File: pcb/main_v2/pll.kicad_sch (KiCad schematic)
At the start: 52 parts, among them U601 ADF4351, U602 XMB0220K1-50100G, U603 PD0922J5050D2HF, Y601 ATX-11-F-26.000MHZ-F05-T

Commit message: updarted schematic and simulation
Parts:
- removed R617: 100, Resistor_SMD:R_0402_1005Metric, symbol Device:R
- removed R618: 200, Resistor_SMD:R_0402_1005Metric, symbol Device:R
- removed U602: XMB0220K1-50100G, My Footprints:XMB0220K1-50100G_TTT, symbol My Symbols:XMB0220K1-50100G
- removed U603: PD0922J5050D2HF, PD0922J5050D2HF, symbol My Symbols:PD0922J5050D2HF
- added C501: 0.1 uF, Capacitor_SMD:C_0402_1005Metric, symbol Device:C
- added C502: 10 pF, Capacitor_SMD:C_0402_1005Metric, symbol Device:C
- added C503: 120 pF, Capacitor_SMD:C_0402_1005Metric, symbol Device:C
- Y601: footprint ATX11F26000MHZF05T -> My Footprints:ATX11F26000MHZF05T
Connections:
- net Vout is gone; now on net +3.3V: C611.1, C612.2, C626.1, L601.1, L602.1
- net +3.3V: now also C501.1, C502.1, C503.2
- net GND: now also C501.2, C502.2, C503.1
- net OX Out + renamed Oscillator +
- net OX Out - renamed Oscillator -
- net RF In renamed TCXO
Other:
- note removed: "Balun 1:2"
- note removed: "Power Splitter"
- note removed: "TODO: calculate loop filter. Welche Bandbreite?"
- moved on the sheet: C613, C627, C628, R605, Y601

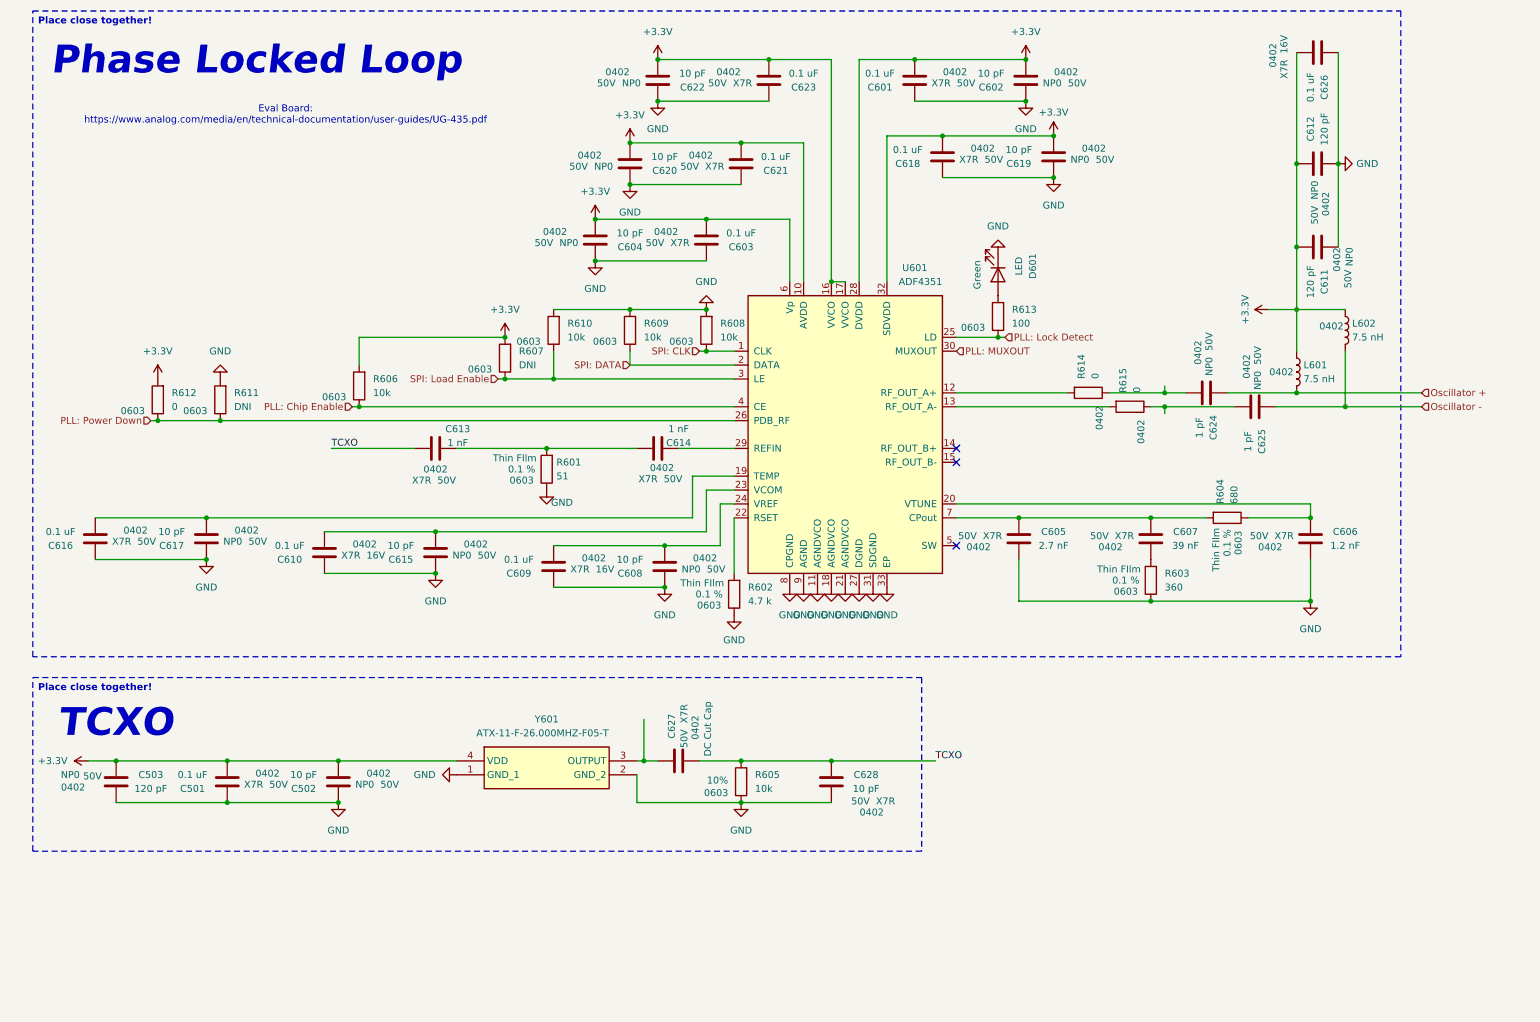
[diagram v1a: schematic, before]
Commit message: updated io schematic
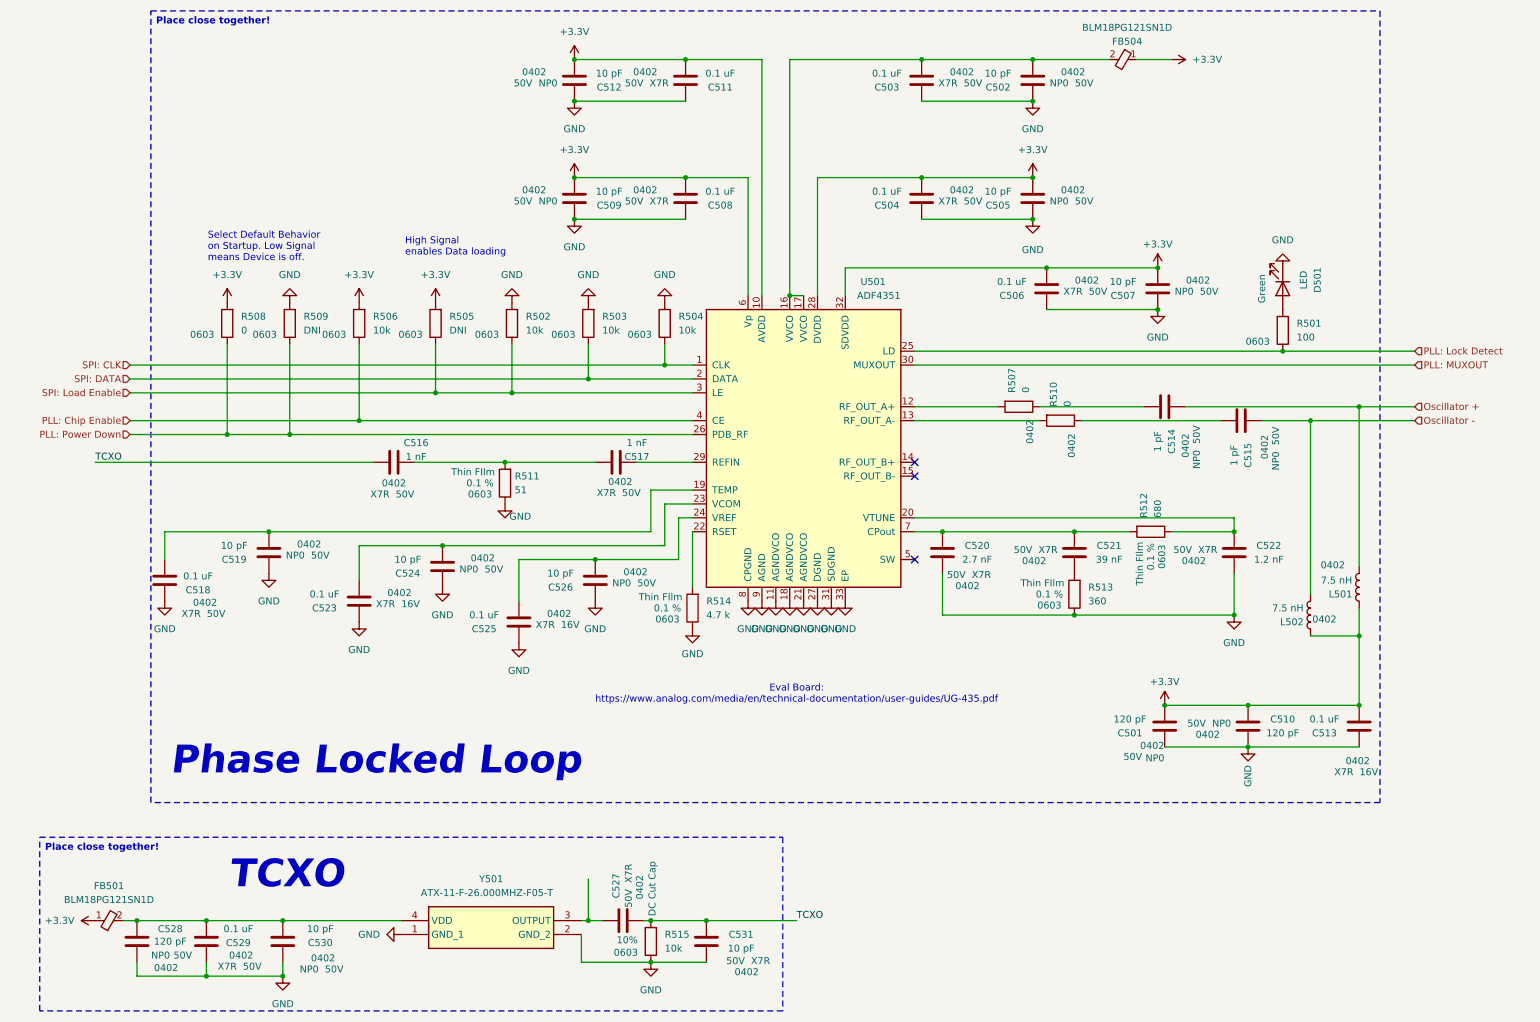
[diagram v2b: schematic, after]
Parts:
- removed C603, C621, C623, C626: 0.1 uF, Capacitor_SMD:C_0402_1005Metric, symbol Device:C
- removed C604, C620, C622: 10 pF, Capacitor_SMD:C_0402_1005Metric, symbol Device:C
- removed C611, C612: 120 pF, Capacitor_SMD:C_0402_1005Metric, symbol Device:C
- removed L601, L602: 7.5 nH, Inductor_SMD:L_0402_1005Metric, symbol Device:L
- added C501, C510: 120 pF, Capacitor_SMD:C_0402_1005Metric, symbol Device:C
- added C502, C509, C512: 10 pF, Capacitor_SMD:C_0402_1005Metric, symbol Device:C
- added C503, C508, C511, C513: 0.1 uF, Capacitor_SMD:C_0402_1005Metric, symbol Device:C
- added FB501, FB504: BLM18PG121SN1D, BLM18SP221SN1B, symbol My Symbols:BLM18PG121SN1D
- added L501, L502: 7.5 nH, Inductor_SMD:L_0402_1005Metric, symbol Device:L
- renumbered C601 to C504, C602 to C505, C618 to C506, C619 to C507, C624 to C514, C625 to C515, C613 to C516, C614 to C517, C616 to C518, C617 to C519, C605 to C520, C607 to C521, C606 to C522, C610 to C523, C615 to C524, C609 to C525, C608 to C526, C627 to C527, C503 to C528, C501 to C529, C502 to C530, C628 to C531, D601 to D501, R613 to R501, R610 to R502, R609 to R503, R608 to R504, R607 to R505, R606 to R506, R614 to R507, R612 to R508, R611 to R509, R615 to R510, R601 to R511, R604 to R512, R603 to R513, R602 to R514, R605 to R515, U601 to U501, Y601 to Y501
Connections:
- net +3.3V: now also C501.1, C508.1, C509.1, C510.2, C511.1, C512.1, C513.1, FB501.1, FB504.1, L501.1, L502.1; no longer C528.2, C529.1, C530.1, U501.16 (VVCO), U501.17 (VVCO), Y501.4 (VDD)
- net GND: now also C501.2, C502.2, C503.2, C508.2, C509.2, C510.1, C511.2, C512.2, C513.2
- net Oscillator +: now also L501.2
- net Oscillator -: now also L502.2
- new net: C502.1, C503.1, FB504.2, U501.16 (VVCO), U501.17 (VVCO)
- new net: C528.2, C529.1, C530.1, FB501.2, Y501.4 (VDD)
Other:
- note added: "High Signal enables Data loading"
- note added: "Select Default Behavior on Startup. Low Signal means Device is off."
- moved on the sheet: C504, C505, C506, C507, C514, C515, C516, C517, C518, C519, C520, C521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

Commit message: update bom
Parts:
- FB501: renamed from FB504; footprint BLM18SP221SN1B -> My Footprints:BLM18SP221SN1B
- FB502: renamed from FB501; footprint BLM18SP221SN1B -> My Footprints:BLM18SP221SN1B
- renumbered C512 to C501, C511 to C502, C502 to C504, C509 to C505, C508 to C506, C504 to C507, C505 to C508, C506 to C509, C507 to C510, C514 to C511, C515 to C512, C516 to C513, C517 to C514, C519 to C515, C520 to C516, C521 to C517, C522 to C518, C524 to C519, C518 to C520, C526 to C521, C523 to C522, C525 to C523, C501 to C524, C510 to C525, C513 to C526, R508 to R501, R509 to R502, R506 to R503, R505 to R504, R502 to R505, R503 to R506, R504 to R507, R501 to R508, R507 to R509

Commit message: updated layout
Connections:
- net Ox Blocked -: now reaches C512.1, R510.1
- net Ox +: now reaches R509.2, U501.12 (RF_OUT_A+)
- net Ox -: now reaches R510.2, U501.13 (RF_OUT_A-)
- net Ox Blocked +: now reaches C511.1, R509.1
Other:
- moved on the sheet: C511, C512

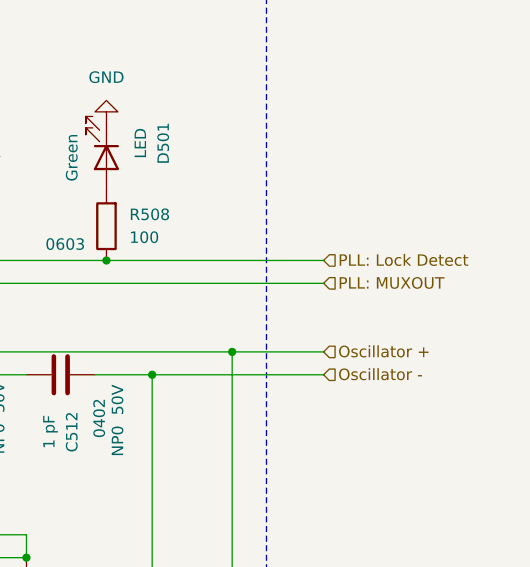
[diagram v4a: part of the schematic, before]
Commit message: updated spi connection
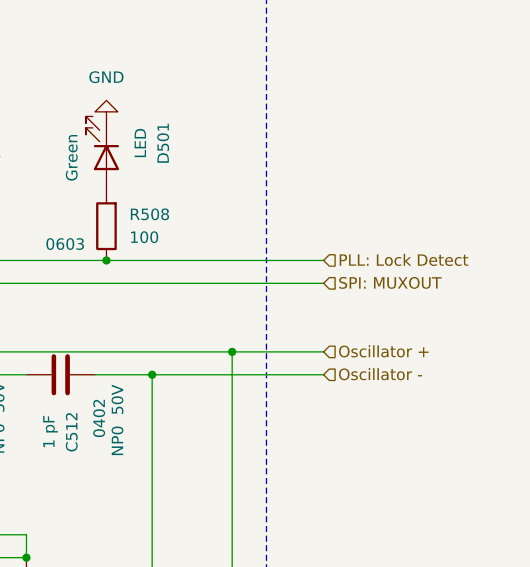
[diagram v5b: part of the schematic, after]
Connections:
- net PLL: MUXOUT renamed SPI: MUXOUT
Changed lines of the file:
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@@
 		)
 	)
-	(hierarchical_label "PLL: MUXOUT"
+	(hierarchical_label "SPI: MUXOUT"
 		(shape input)
 		(at 266.7 77.47 0)

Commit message: added second LNA
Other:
- note added: "Place Thermal Vias for Heat Dissapation!"
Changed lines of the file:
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@@
 		)
 	)
+	(text "Place Thermal Vias for Heat Dissapation!"
+		(exclude_from_sim no)
+		(at 62.738 26.162 0)
+		(effects
+			(font
+				(size 1.27 1.27)
+			)
+		)
+	)
 	(text "High Signal \nenables Data loading\n"
 		(exclude_from_sim no)
@@
 					(unit 1)
 				)
+			)
+		)
+	)
+	(symbol
+		(lib_id "Graphic:SYM_Hot_Small")
+		(at 62.23 30.48 0)
+		(unit 1)
+		(body_style 1)
+		(exclude_from_sim yes)
+		(in_bom no)
+		(on_board no)
+		(in_pos_files yes)
+		(dnp no)
+		(fields_autoplaced yes)
+		(property "Reference" "#SYM501"
+			(at 62.23 26.924 0)
+			(hide yes)
+			(show_name no)
+			(do_not_autoplace no)
+			(effects
+				(font
+					(size 1.27 1.27)
+				)
+			)
+		)
+		(property "Value" "SYM_Hot_Small"
+			(at 62.23 33.655 0)
+			(hide yes)
+			(show_name no)
+			(do_not_autoplace no)
+			(effects
+				(font
+					(size 1.27 1.27)
+				)
+			)
+		)
+		(property "Footprint" ""
+			(at 62.23 34.925 0)
+			(hide yes)
+			(show_name no)
+			(do_not_autoplace no)
+			(effects
+				(font
+					(size 1.27 1.27)
+				)
+			)
+		)
+		(property "Datasheet" ""
+			(at 62.992 35.56 0)
+			(hide yes)
+			(show_name no)
+			(do_not_autoplace no)
+			(effects
+				(font
+					(size 1.27 1.27)
+				)
+			)
+		)
+		(property "Description" "Hot surface warning symbol, small"
+			(at 62.23 30.48 0)
+			(hide yes)
+			(show_name no)
+			(do_not_autoplace no)
+			(effects
+				(font
+					(size 1.27 1.27)
+				)
+			)
+		)
+		(instances
+			(project "main_v2"
+				(path "/0599865e-4bed-44f1-b46e-4b55335b49b2/87c8c23a-5063-4def-b6c3-72078f0eafd4"
+					(reference "#SYM501")
+					(unit 1)
+				)

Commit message: added new doc files
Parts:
- C527: value DC Cut Cap -> 1nF
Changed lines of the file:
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@@
 			)
 		)
-		(property "Value" "DC Cut Cap"
+		(property "Value" "1nF"
 			(at 127.254 173.228 0)
 			(show_name no)
